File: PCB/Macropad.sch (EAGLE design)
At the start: 84 parts, among them IC1 LM2937, J1 54819-0519

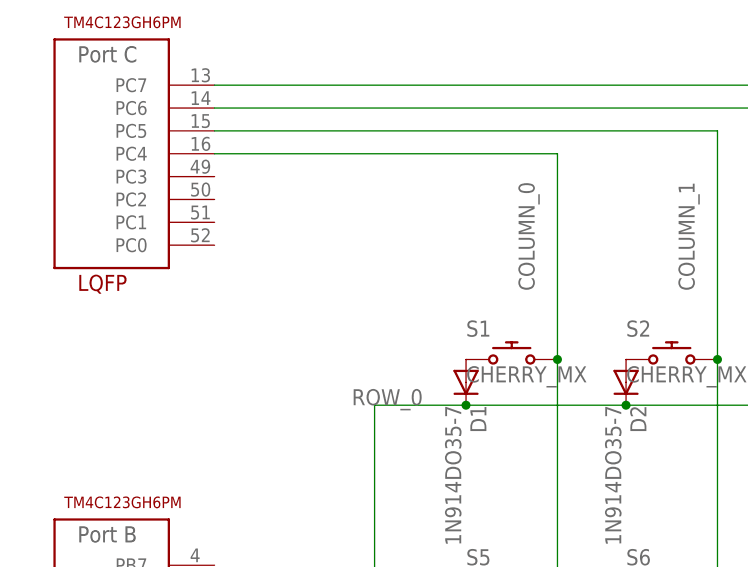
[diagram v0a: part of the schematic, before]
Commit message: Added JTAG connection
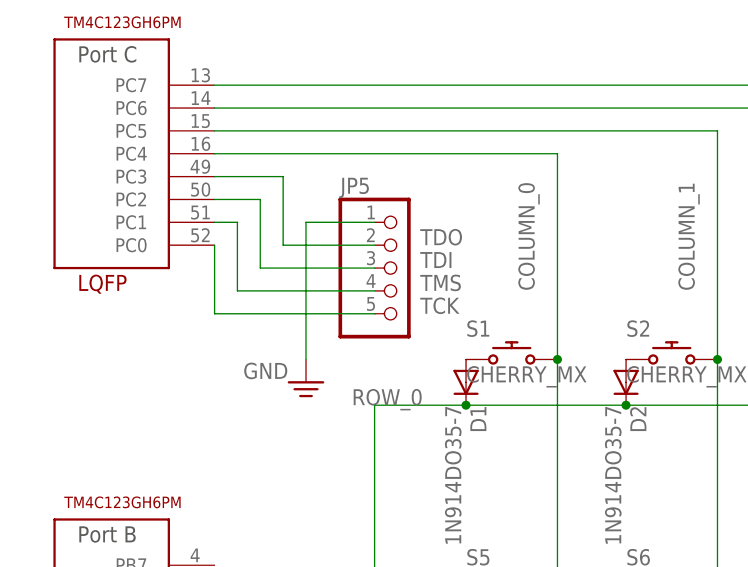
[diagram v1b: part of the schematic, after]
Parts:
- added JP5: (no value), EE445L:PINHD-1X5
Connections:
- new net TCK: JP5.5, U$1G$3.PC0
- new net TDI: JP5.3, U$1G$3.PC2
- new net TDO: JP5.2, U$1G$3.PC3
- new net TMS: JP5.4, U$1G$3.PC1
- net GND: now also JP5.1
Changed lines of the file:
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@@
 <part name="JP3" library="EE445L" deviceset="PINHD-1X4" device=""/>
 <part name="JP4" library="EE445L" deviceset="PINHD-1X5" device=""/>
+<part name="JP5" library="EE445L" deviceset="PINHD-1X5" device=""/>
+<part name="SUPPLY7" library="EE445L" deviceset="GND" device=""/>
 </parts>
 <sheets>
@@
 <attribute name="NAME" x="191.77" y="356.235" size="1.778" layer="95"/>
 <attribute name="VALUE" x="191.77" y="337.82" size="1.778" layer="96"/>
+</instance>
+<instance part="JP5" gate="A" x="58.42" y="401.32" smashed="yes">
+<attribute name="NAME" x="52.07" y="409.575" size="1.778" layer="95"/>
+<attribute name="VALUE" x="52.07" y="391.16" size="1.778" layer="96"/>
+</instance>
+<instance part="SUPPLY7" gate="GND" x="48.26" y="388.62" smashed="yes">
+<attribute name="VALUE" x="41.275" y="389.001" size="1.778" layer="96"/>
 </instance>
 </instances>
@@
 <pinref part="J1" gate="G$1" pin="GND"/>
 <wire x1="398.78" y1="106.68" x2="408.94" y2="106.68" width="0.1524" layer="91"/>
+</segment>
+<segment>
+<pinref part="JP5" gate="A" pin="1"/>
+<wire x1="55.88" y1="406.4" x2="48.26" y2="406.4" width="0.1524" layer="91"/>
+<pinref part="SUPPLY7" gate="GND" pin="GND"/>
+<wire x1="48.26" y1="391.16" x2="48.26" y2="406.4" width="0.1524" layer="91"/>
 </segment>
 </net>
@@
 </segment>
 </net>
+<net name="TDO" class="0">
+<segment>
+<pinref part="U$1" gate="G$3" pin="PC3"/>
+<wire x1="38.1" y1="411.48" x2="45.72" y2="411.48" width="0.1524" layer="91"/>
+<wire x1="45.72" y1="411.48" x2="45.72" y2="403.86" width="0.1524" layer="91"/>
+<pinref part="JP5" gate="A" pin="2"/>
+<wire x1="45.72" y1="403.86" x2="55.88" y2="403.86" width="0.1524" layer="91"/>
+<label x="60.96" y="403.86" size="1.778" layer="95"/>
+</segment>
+</net>
+<net name="TDI" class="0">
+<segment>
+<pinref part="U$1" gate="G$3" pin="PC2"/>
+<wire x1="38.1" y1="408.94" x2="43.18" y2="408.94" width="0.1524" layer="91"/>
+<wire x1="43.18" y1="408.94" x2="43.18" y2="401.32" width="0.1524" layer="91"/>
+<pinref part="JP5" gate="A" pin="3"/>
+<wire x1="43.18" y1="401.32" x2="55.88" y2="401.32" width="0.1524" layer="91"/>
+<label x="60.96" y="401.32" size="1.778" layer="95"/>
+</segment>
+</net>
+<net name="TMS" class="0">
+<segment>
+<pinref part="U$1" gate="G$3" pin="PC1"/>
+<wire x1="38.1" y1="406.4" x2="40.64" y2="406.4" width="0.1524" layer="91"/>
+<pinref part="JP5" gate="A" pin="4"/>
+<wire x1="40.64" y1="406.4" x2="40.64" y2="398.78" width="0.1524" layer="91"/>
+<wire x1="40.64" y1="398.78" x2="55.88" y2="398.78" width="0.1524" layer="91"/>
+<label x="60.96" y="398.78" size="1.778" layer="95"/>
+</segment>
+</net>
+<net name="TCK" class="0">
+<segment>
+<pinref part="U$1" gate="G$3" pin="PC0"/>
+<wire x1="38.1" y1="403.86" x2="38.1" y2="396.24" width="0.1524" layer="91"/>
+<pinref part="JP5" gate="A" pin="5"/>
+<wire x1="38.1" y1="396.24" x2="55.88" y2="396.24" width="0.1524" layer="91"/>
+<label x="60.96" y="396.24" size="1.778" layer="95"/>
+</segment>
+</net>

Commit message: Started pcb layout
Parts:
- removed 3.3V, 5.0V, GND, GND1: TP_LOOP, EE445L:TP_LOOP
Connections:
- net N$1 renamed OSC1
- net N$2 renamed OSC0
- net N$5 renamed +5V_POWER
- net N$7 renamed LED_IN
- net N$8 renamed RESET
- net N$9 renamed WAKE
- net +3V3: no longer 3.3V.TP
- net +5V: no longer 5.0V.TP
- net GND: no longer GND.TP, GND1.TP
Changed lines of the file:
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@@
 <part name="FRAME1" library="frames" library_urn="urn:adsk.eagle:library:229" deviceset="FRAME_A_L" device=""/>
 <part name="FRAME2" library="frames" library_urn="urn:adsk.eagle:library:229" deviceset="FRAME_A_L" device=""/>
-<part name="5.0V" library="EE445L" deviceset="TP_LOOP" device=""/>
 <part name="U$4" library="EE445L" deviceset="POWER_CONN" device=""/>
-<part name="GND" library="EE445L" deviceset="TP_LOOP" device=""/>
 <part name="JP2" library="EE445L" deviceset="PINHD-1X2" device=""/>
 <part name="IC1" library="EE445L" deviceset="LM2937" device=""/>
 <part name="C16" library="EE445L" deviceset="CAPACITOR_POLARIZED" device="E5-6" value="4.7uf"/>
-<part name="3.3V" library="EE445L" deviceset="TP_LOOP" device=""/>
 <part name="C17" library="EE445L" deviceset="CAPACITOR_POLARIZED" device="E5-6" value="4.7uf"/>
 <part name="+3V3" library="EE445L" deviceset="+3V3" device=""/>
@@
 <part name="+3V5" library="EE445L" deviceset="+3V3" device=""/>
 <part name="R4" library="EE445L" deviceset="RESISTOR" device="0204/5" value="1M"/>
-<part name="GND1" library="EE445L" deviceset="TP_LOOP" device=""/>
 <part name="C18" library="EE445L" deviceset="CAPACITOR" device="025-024X044" value="0.1uf"/>
 <part name="SUPPLY20" library="EE445L" deviceset="GND" device=""/>
@@
 <attribute name="DRAWING_NAME" x="480.06" y="19.05" size="2.54" layer="94"/>
 </instance>
-<instance part="5.0V" gate="G$1" x="78.74" y="195.58" smashed="yes">
-<attribute name="NAME" x="76.2" y="198.628" size="1.778" layer="95"/>
-</instance>
 <instance part="U$4" gate="G$1" x="20.32" y="170.18" smashed="yes"/>
-<instance part="GND" gate="G$1" x="45.72" y="147.32" smashed="yes" rot="R180">
-<attribute name="NAME" x="48.26" y="144.272" size="1.778" layer="95" rot="R180"/>
-</instance>
 <instance part="JP2" gate="G$1" x="53.34" y="193.04" smashed="yes" rot="R90">
 <attribute name="NAME" x="50.165" y="194.31" size="1.778" layer="95" align="bottom-center"/>
@@
 <attribute name="NAME" x="67.056" y="178.435" size="1.778" layer="95"/>
 <attribute name="VALUE" x="59.436" y="173.609" size="1.778" layer="96"/>
-</instance>
-<instance part="3.3V" gate="G$1" x="116.84" y="195.58" smashed="yes">
-<attribute name="NAME" x="114.3" y="198.628" size="1.778" layer="95"/>
 </instance>
 <instance part="C17" gate="G$1" x="111.76" y="177.8" smashed="yes">
@@
 <attribute name="NAME" x="140.97" y="97.5614" size="1.778" layer="95" rot="R180"/>
 <attribute name="VALUE" x="140.97" y="102.362" size="1.778" layer="96" rot="R180"/>
-</instance>
-<instance part="GND1" gate="G$1" x="106.68" y="147.32" smashed="yes" rot="R180">
-<attribute name="NAME" x="109.22" y="144.272" size="1.778" layer="95" rot="R180"/>
 </instance>
 <instance part="C18" gate="G$1" x="240.03" y="100.33" smashed="yes">
@@
 <pinref part="C17" gate="G$1" pin="-"/>
 <wire x1="111.76" y1="172.72" x2="111.76" y2="160.02" width="0.1524" layer="91"/>
-<wire x1="111.76" y1="160.02" x2="106.68" y2="160.02" width="0.1524" layer="91"/>
 <junction x="96.52" y="160.02"/>
-<wire x1="106.68" y1="160.02" x2="96.52" y2="160.02" width="0.1524" layer="91"/>
+<wire x1="111.76" y1="160.02" x2="96.52" y2="160.02" width="0.1524" layer="91"/>
 <wire x1="111.76" y1="160.02" x2="132.08" y2="160.02" width="0.1524" layer="91"/>
 <junction x="111.76" y="160.02"/>
 <pinref part="U$4" gate="G$1" pin="GND"/>
 <wire x1="22.86" y1="167.64" x2="22.86" y2="160.02" width="0.1524" layer="91"/>
-<wire x1="22.86" y1="160.02" x2="45.72" y2="160.02" width="0.1524" layer="91"/>
-<pinref part="GND" gate="G$1" pin="TP"/>
-<wire x1="45.72" y1="160.02" x2="66.04" y2="160.02" width="0.1524" layer="91"/>
-<wire x1="45.72" y1="152.4" x2="45.72" y2="160.02" width="0.1524" layer="91"/>
-<junction x="45.72" y="160.02"/>
+<wire x1="22.86" y1="160.02" x2="66.04" y2="160.02" width="0.1524" layer="91"/>
 <pinref part="SUPPLY11" gate="GND" pin="GND"/>
 <wire x1="83.82" y1="152.4" x2="83.82" y2="160.02" width="0.1524" layer="91"/>
@@
 <pinref part="LED2" gate="G$1" pin="C"/>
 <wire x1="132.08" y1="162.56" x2="132.08" y2="160.02" width="0.1524" layer="91"/>
-<pinref part="GND1" gate="G$1" pin="TP"/>
-<wire x1="106.68" y1="152.4" x2="106.68" y2="160.02" width="0.1524" layer="91"/>
-<junction x="106.68" y="160.02"/>
 </segment>
 <segment>
@@
 <wire x1="137.16" y1="187.96" x2="137.16" y2="185.42" width="0.1524" layer="91"/>
 <pinref part="IC1" gate="G$1" pin="VO"/>
-<pinref part="3.3V" gate="G$1" pin="TP"/>
 <wire x1="106.68" y1="185.42" x2="111.76" y2="185.42" width="0.1524" layer="91"/>
-<wire x1="111.76" y1="185.42" x2="116.84" y2="185.42" width="0.1524" layer="91"/>
-<wire x1="116.84" y1="185.42" x2="116.84" y2="190.5" width="0.1524" layer="91"/>
-<junction x="116.84" y="185.42"/>
 <pinref part="C17" gate="G$1" pin="+"/>
 <wire x1="137.16" y1="185.42" x2="132.08" y2="185.42" width="0.1524" layer="91"/>
-<wire x1="132.08" y1="185.42" x2="116.84" y2="185.42" width="0.1524" layer="91"/>
+<wire x1="132.08" y1="185.42" x2="111.76" y2="185.42" width="0.1524" layer="91"/>
 <wire x1="111.76" y1="180.34" x2="111.76" y2="185.42" width="0.1524" layer="91"/>
 <junction x="111.76" y="185.42"/>
@@
 <segment>
 <pinref part="JP2" gate="G$1" pin="2"/>
-<pinref part="5.0V" gate="G$1" pin="TP"/>
 <wire x1="53.34" y1="190.5" x2="53.34" y2="185.42" width="0.1524" layer="91"/>
 <wire x1="53.34" y1="185.42" x2="66.04" y2="185.42" width="0.1524" layer="91"/>
 <wire x1="66.04" y1="185.42" x2="68.58" y2="185.42" width="0.1524" layer="91"/>
-<wire x1="68.58" y1="185.42" x2="78.74" y2="185.42" width="0.1524" layer="91"/>
-<wire x1="78.74" y1="185.42" x2="78.74" y2="190.5" width="0.1524" layer="91"/>
+<wire x1="68.58" y1="185.42" x2="86.36" y2="185.42" width="0.1524" layer="91"/>
 <label x="60.96" y="187.96" size="1.778" layer="95" align="top-center"/>
 <pinref part="IC1" gate="G$1" pin="VI"/>
-<wire x1="86.36" y1="185.42" x2="78.74" y2="185.42" width="0.1524" layer="91"/>
-<junction x="78.74" y="185.42"/>
 <pinref part="C16" gate="G$1" pin="+"/>
 <wire x1="66.04" y1="180.34" x2="66.04" y2="185.42" width="0.1524" layer="91"/>
@@
 </segment>
 </net>
-<net name="N$5" class="0">
+<net name="+5V_POWER" class="0">
 <segment>
 <pinref part="U$4" gate="G$1" pin="VDD"/>
@@
 <wire x1="50.8" y1="185.42" x2="50.8" y2="190.5" width="0.1524" layer="91"/>
 <wire x1="22.86" y1="185.42" x2="43.18" y2="185.42" width="0.1524" layer="91"/>
+<label x="27.94" y="185.42" size="1.778" layer="95"/>
 </segment>
 </net>
-<net name="N$7" class="0">
+<net name="LED_IN" class="0">
 <segment>
 <pinref part="R1" gate="G$1" pin="1"/>
@@
 </segment>
 </net>
-<net name="N$8" class="0">
+<net name="RESET" class="0">
 <segment>
 <pinref part="RESET" gate="1" pin="S"/>
@@
 </segment>
 </net>
-<net name="N$1" class="0">
+<net name="OSC1" class="0">
 <segment>
 <pinref part="U$1" gate="G$7" pin="OSC1"/>
@@
 </segment>
 </net>
-<net name="N$2" class="0">
+<net name="OSC0" class="0">
 <segment>
 <pinref part="U$2" gate="G$1" pin="P$1"/>
@@
 </segment>
 </net>
-<net name="N$9" class="0">
+<net name="WAKE" class="0">
 <segment>
 <pinref part="U$1" gate="G$7" pin="!WAKE"/>

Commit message: Added rotary encoder
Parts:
- added U1: EC11E09244AQ, SamacSys_Parts:EC11E09244AQ
- renumbered JP5 to JTAG
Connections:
- net GND: now also J1.SHIELD, U1.NO, U1.WIPER
- net PF0: now also U1.CW
- net PF1: now also U1.CCW
- net PF2: now also U1.COM
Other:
- moved on the sheet: JP4
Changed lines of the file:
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@@
 <part name="JP3" library="EE445L" deviceset="PINHD-1X4" device=""/>
 <part name="JP4" library="EE445L" deviceset="PINHD-1X5" device=""/>
-<part name="JP5" library="EE445L" deviceset="PINHD-1X5" device=""/>
+<part name="JTAG" library="EE445L" deviceset="PINHD-1X5" device=""/>
 <part name="SUPPLY7" library="EE445L" deviceset="GND" device=""/>
+<part name="U1" library="SamacSys_Parts" deviceset="EC11E09244AQ" device=""/>
+<part name="SUPPLY8" library="EE445L" deviceset="GND" device=""/>
+<part name="SUPPLY9" library="EE445L" deviceset="GND" device=""/>
 </parts>
 <sheets>
@@
 <attribute name="VALUE" x="163.83" y="393.7" size="1.778" layer="96"/>
 </instance>
-<instance part="U$1" gate="G$6" x="157.48" y="340.36" smashed="yes"/>
-<instance part="JP4" gate="A" x="198.12" y="347.98" smashed="yes">
-<attribute name="NAME" x="191.77" y="356.235" size="1.778" layer="95"/>
-<attribute name="VALUE" x="191.77" y="337.82" size="1.778" layer="96"/>
-</instance>
-<instance part="JP5" gate="A" x="58.42" y="401.32" smashed="yes">
+<instance part="U$1" gate="G$6" x="396.24" y="60.96" smashed="yes"/>
+<instance part="JP4" gate="A" x="436.88" y="68.58" smashed="yes">
+<attribute name="NAME" x="430.53" y="76.835" size="1.778" layer="95"/>
+<attribute name="VALUE" x="430.53" y="58.42" size="1.778" layer="96"/>
+</instance>
+<instance part="JTAG" gate="A" x="58.42" y="401.32" smashed="yes">
 <attribute name="NAME" x="52.07" y="409.575" size="1.778" layer="95"/>
 <attribute name="VALUE" x="52.07" y="391.16" size="1.778" layer="96"/>
@@
 <instance part="SUPPLY7" gate="GND" x="48.26" y="388.62" smashed="yes">
 <attribute name="VALUE" x="41.275" y="389.001" size="1.778" layer="96"/>
+</instance>
+<instance part="U1" gate="G$1" x="337.82" y="58.42" smashed="yes">
+<attribute name="NAME" x="359.41" y="73.66" size="1.778" layer="95" align="center-left"/>
+<attribute name="VALUE" x="359.41" y="71.12" size="1.778" layer="96" align="center-left"/>
+</instance>
+<instance part="SUPPLY8" gate="GND" x="350.52" y="27.94" smashed="yes">
+<attribute name="VALUE" x="346.075" y="23.241" size="1.778" layer="96"/>
+</instance>
+<instance part="SUPPLY9" gate="GND" x="350.52" y="81.28" smashed="yes" rot="R180">
+<attribute name="VALUE" x="354.965" y="85.979" size="1.778" layer="96" rot="R180"/>
 </instance>
 </instances>
@@
 <pinref part="SUPPLY6" gate="GND" pin="GND"/>
 <pinref part="J1" gate="G$1" pin="GND"/>
-<wire x1="398.78" y1="106.68" x2="408.94" y2="106.68" width="0.1524" layer="91"/>
-</segment>
-<segment>
-<pinref part="JP5" gate="A" pin="1"/>
+<wire x1="398.78" y1="106.68" x2="403.86" y2="106.68" width="0.1524" layer="91"/>
+<wire x1="403.86" y1="106.68" x2="408.94" y2="106.68" width="0.1524" layer="91"/>
+<wire x1="403.86" y1="106.68" x2="403.86" y2="101.6" width="0.1524" layer="91"/>
+<junction x="403.86" y="106.68"/>
+<pinref part="J1" gate="G$1" pin="SHIELD"/>
+<wire x1="403.86" y1="101.6" x2="408.94" y2="101.6" width="0.1524" layer="91"/>
+</segment>
+<segment>
+<pinref part="JTAG" gate="A" pin="1"/>
 <wire x1="55.88" y1="406.4" x2="48.26" y2="406.4" width="0.1524" layer="91"/>
 <pinref part="SUPPLY7" gate="GND" pin="GND"/>
 <wire x1="48.26" y1="391.16" x2="48.26" y2="406.4" width="0.1524" layer="91"/>
+</segment>
+<segment>
+<pinref part="U1" gate="G$1" pin="WIPER"/>
+<pinref part="SUPPLY8" gate="GND" pin="GND"/>
+<wire x1="350.52" y1="30.48" x2="350.52" y2="40.64" width="0.1524" layer="91"/>
+</segment>
+<segment>
+<pinref part="U1" gate="G$1" pin="NO"/>
+<pinref part="SUPPLY9" gate="GND" pin="GND"/>
+<wire x1="350.52" y1="73.66" x2="350.52" y2="78.74" width="0.1524" layer="91"/>
 </segment>
 </net>
@@
 <pinref part="U$1" gate="G$6" pin="PF4"/>
 <pinref part="JP4" gate="A" pin="1"/>
-<wire x1="175.26" y1="353.06" x2="195.58" y2="353.06" width="0.1524" layer="91"/>
+<wire x1="414.02" y1="73.66" x2="434.34" y2="73.66" width="0.1524" layer="91"/>
 </segment>
 </net>
@@
 <pinref part="U$1" gate="G$6" pin="PF3"/>
 <pinref part="JP4" gate="A" pin="2"/>
-<wire x1="175.26" y1="350.52" x2="195.58" y2="350.52" width="0.1524" layer="91"/>
+<wire x1="414.02" y1="71.12" x2="434.34" y2="71.12" width="0.1524" layer="91"/>
 </segment>
 </net>
@@
 <pinref part="U$1" gate="G$6" pin="PF2"/>
 <pinref part="JP4" gate="A" pin="3"/>
-<wire x1="175.26" y1="347.98" x2="195.58" y2="347.98" width="0.1524" layer="91"/>
+<wire x1="414.02" y1="68.58" x2="434.34" y2="68.58" width="0.1524" layer="91"/>
+</segment>
+<segment>
+<pinref part="U1" gate="G$1" pin="COM"/>
+<wire x1="347.98" y1="73.66" x2="347.98" y2="78.74" width="0.1524" layer="91"/>
+<label x="342.9" y="78.74" size="1.778" layer="95"/>
 </segment>
 </net>
@@
 <pinref part="U$1" gate="G$6" pin="PF1"/>
 <pinref part="JP4" gate="A" pin="4"/>
-<wire x1="175.26" y1="345.44" x2="195.58" y2="345.44" width="0.1524" layer="91"/>
+<wire x1="414.02" y1="66.04" x2="434.34" y2="66.04" width="0.1524" layer="91"/>
+</segment>
+<segment>
+<pinref part="U1" gate="G$1" pin="CCW"/>
+<wire x1="353.06" y1="40.64" x2="353.06" y2="38.1" width="0.1524" layer="91"/>
+<label x="353.06" y="35.56" size="1.778" layer="95"/>
 </segment>
 </net>
@@
 <pinref part="U$1" gate="G$6" pin="PF0"/>
 <pinref part="JP4" gate="A" pin="5"/>
-<wire x1="175.26" y1="342.9" x2="195.58" y2="342.9" width="0.1524" layer="91"/>
+<wire x1="414.02" y1="63.5" x2="434.34" y2="63.5" width="0.1524" layer="91"/>
+</segment>
+<segment>
+<pinref part="U1" gate="G$1" pin="CW"/>
+<wire x1="347.98" y1="40.64" x2="347.98" y2="38.1" width="0.1524" layer="91"/>
+<label x="345.44" y="35.56" size="1.778" layer="95"/>
 </segment>
 </net>
@@
 <wire x1="38.1" y1="411.48" x2="45.72" y2="411.48" width="0.1524" layer="91"/>
 <wire x1="45.72" y1="411.48" x2="45.72" y2="403.86" width="0.1524" layer="91"/>
-<pinref part="JP5" gate="A" pin="2"/>
+<pinref part="JTAG" gate="A" pin="2"/>
 <wire x1="45.72" y1="403.86" x2="55.88" y2="403.86" width="0.1524" layer="91"/>
 <label x="60.96" y="403.86" size="1.778" layer="95"/>
@@
 <wire x1="38.1" y1="408.94" x2="43.18" y2="408.94" width="0.1524" layer="91"/>
 <wire x1="43.18" y1="408.94" x2="43.18" y2="401.32" width="0.1524" layer="91"/>
-<pinref part="JP5" gate="A" pin="3"/>
+<pinref part="JTAG" gate="A" pin="3"/>
 <wire x1="43.18" y1="401.32" x2="55.88" y2="401.32" width="0.1524" layer="91"/>
 <label x="60.96" y="401.32" size="1.778" layer="95"/>
@@
 <pinref part="U$1" gate="G$3" pin="PC1"/>
 <wire x1="38.1" y1="406.4" x2="40.64" y2="406.4" width="0.1524" layer="91"/>
-<pinref part="JP5" gate="A" pin="4"/>
+<pinref part="JTAG" gate="A" pin="4"/>
 <wire x1="40.64" y1="406.4" x2="40.64" y2="398.78" width="0.1524" layer="91"/>
 <wire x1="40.64" y1="398.78" x2="55.88" y2="398.78" width="0.1524" layer="91"/>
@@
 <pinref part="U$1" gate="G$3" pin="PC0"/>
 <wire x1="38.1" y1="403.86" x2="38.1" y2="396.24" width="0.1524" layer="91"/>
-<pinref part="JP5" gate="A" pin="5"/>
+<pinref part="JTAG" gate="A" pin="5"/>
 <wire x1="38.1" y1="396.24" x2="55.88" y2="396.24" width="0.1524" layer="91"/>
 <label x="60.96" y="396.24" size="1.778" layer="95"/>

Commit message: Finished first draft of PCB layout
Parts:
- removed D3, D4: 1N914DO35-7, EE445L:1N914DO35-7
- removed J1: 54819-0519, 54819-0519:54819-0519
- removed JP2: (no value), EE445L:PINHD-1X2
- removed LED2: (no value), EE445L:LED3MM
- removed R1: 1K, EE445L:RESISTOR0204/5
- removed S3, S4: CHERRY_MX, cherry:CHERRY_MX
- removed U$4: POWER_CONN, EE445L:POWER_CONN
- added X1: ZX62D-B-5PA8, zx62d-b-5pa8-oshpark_10:ZX62D-B-5PA8
- renumbered JP1 to ROWS, JP3 to COLUMNS
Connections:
- removed net +5V_POWER: JP2.1, U$4.VDD
- removed net COLUMN_4: ROWS.5
- removed net COLUMN_5: ROWS.6
- removed net LED_IN: LED2.A, R1.1
- removed net N$10: D4.A, S4.1
- removed net N$6: D3.A, S3.1
- removed net PF4: JP4.1, U$1G$6.PF4
- net +3V3: no longer R1.2
- net +5V: now also X1G$1.1; no longer J1.VBUS, JP2.2
- net COLUMN_0: now also COLUMNS.1; no longer ROWS.1
- net COLUMN_1: now also COLUMNS.2; no longer ROWS.2
- net COLUMN_2: now also COLUMNS.3; no longer ROWS.3, S3.2
- net COLUMN_3: now also COLUMNS.4; no longer ROWS.4, S4.2
- net D+: now also X1G$1.3; no longer J1.D+
- net D-: now also X1G$1.2; no longer J1.D-
- net GND: now also X1G$1.5; no longer J1.GND, J1.SHIELD, LED2.C, U$4.GND
- net ROW_0: now also ROWS.1; no longer COLUMNS.1, D3.C, D4.C
- net ROW_1: now also ROWS.2; no longer COLUMNS.2
- net ROW_2: now also ROWS.3; no longer COLUMNS.3
- net ROW_3: now also ROWS.4; no longer COLUMNS.4
- net ROW_4: now also ROWS.5
- net ROW_5: now also ROWS.6
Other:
- note removed: "Use this jumper to measure current"
